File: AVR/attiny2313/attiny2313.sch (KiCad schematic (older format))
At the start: 7 parts

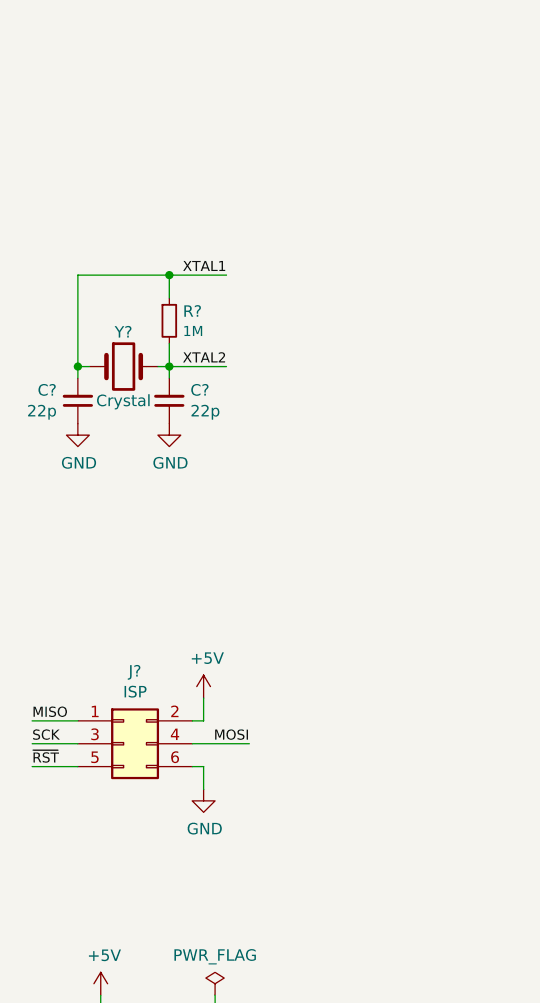
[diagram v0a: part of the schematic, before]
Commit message: Improving AVR templates
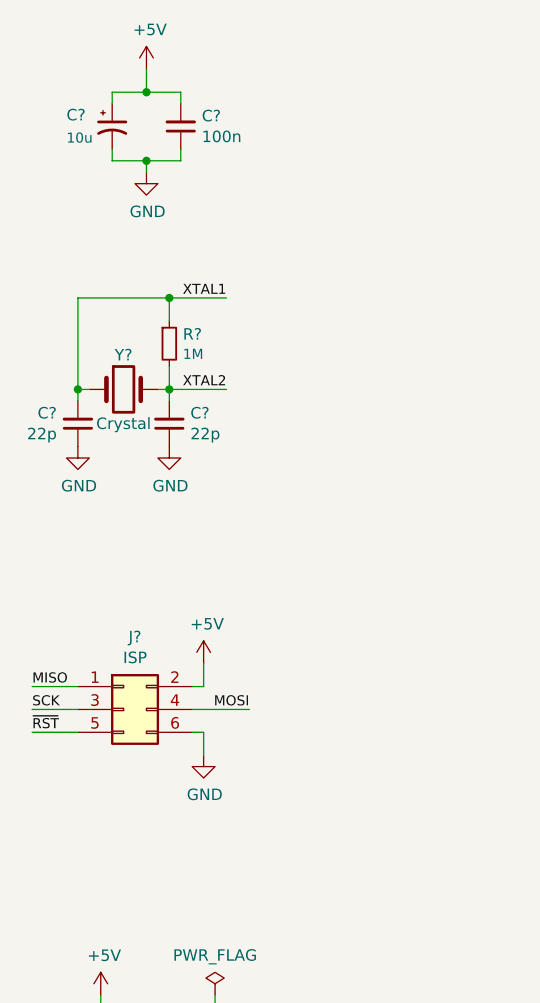
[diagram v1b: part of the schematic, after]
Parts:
- added C?: 10u, symbol Device:CP1_Small
- added C?: 100n, symbol Device:C_Small
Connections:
- net +5V: now also C?.1, C?.2
- net GND: now also C?.1, C?.2
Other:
- moved on the sheet: C?, J?, R?, Y?
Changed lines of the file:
@@
 EESchema Schematic File Version 4
-LIBS:atmega8-cache
+LIBS:attiny2313-cache
 EELAYER 26 0
 EELAYER END
@@
 $EndDescr
 Wire Wire Line
-	1750 2950 1700 2950
-Wire Wire Line
-	2100 2850 2100 2950
-Connection ~ 2100 2950
-Connection ~ 1700 2950
-Wire Wire Line
-	2050 2950 2100 2950
-Text Label 2350 2550 2    44   ~ 0
+	1750 3050 1700 3050
+Wire Wire Line
+	2100 2950 2100 3050
+Connection ~ 2100 3050
+Connection ~ 1700 3050
+Wire Wire Line
+	2050 3050 2100 3050
+Text Label 2350 2650 2    44   ~ 0
 XTAL1
-Text Label 2350 2950 2    44   ~ 0
+Text Label 2350 3050 2    44   ~ 0
 XTAL2
 Wire Wire Line
-	1700 2550 1700 2950
-Wire Wire Line
-	2350 2550 2100 2550
-Wire Wire Line
-	2100 2650 2100 2550
-Connection ~ 2100 2550
-Wire Wire Line
-	2100 2950 2100 3000
-Wire Wire Line
-	2100 2950 2350 2950
-Wire Wire Line
-	1700 2950 1700 3000
-Wire Wire Line
-	2100 2550 1700 2550
+	1700 2650 1700 3050
+Wire Wire Line
+	2350 2650 2100 2650
+Wire Wire Line
+	2100 2750 2100 2650
+Connection ~ 2100 2650
+Wire Wire Line
+	2100 3050 2100 3100
+Wire Wire Line
+	2100 3050 2350 3050
+Wire Wire Line
+	1700 3050 1700 3100
+Wire Wire Line
+	2100 2650 1700 2650
 $Comp
 L Device:Crystal Y?
 U 1 1 5B7974AC
-P 1900 2950
-F 0 "Y?" H 1900 3100 50  0000 C CNN
-F 1 "Crystal" H 1900 2800 50  0000 C CNN
-F 2 "" H 1900 2950 50  0001 C CNN
-F 3 "~" H 1900 2950 50  0001 C CNN
-	1    1900 2950
+P 1900 3050
+F 0 "Y?" H 1900 3200 50  0000 C CNN
+F 1 "Crystal" H 1900 2900 50  0000 C CNN
+F 2 "" H 1900 3050 50  0001 C CNN
+F 3 "~" H 1900 3050 50  0001 C CNN
+	1    1900 3050
 	1    0    0    -1
 $EndComp
@@
 L power:GND #PWR?
 U 1 1 5B79740B
-P 1700 3200
-F 0 "#PWR?" H 1700 2950 50  0001 C CNN
-F 1 "GND" H 1705 3027 50  0000 C CNN
-F 2 "" H 1700 3200 50  0001 C CNN
-F 3 "" H 1700 3200 50  0001 C CNN
-	1    1700 3200
+P 1700 3300
+F 0 "#PWR?" H 1700 3050 50  0001 C CNN
+F 1 "GND" H 1705 3127 50  0000 C CNN
+F 2 "" H 1700 3300 50  0001 C CNN
+F 3 "" H 1700 3300 50  0001 C CNN
+	1    1700 3300
 	1    0    0    -1
 $EndComp
@@
 L Device:C_Small C?
 U 1 1 5B7975FD
-P 1700 3100
-F 0 "C?" H 1608 3054 50  0000 R CNN
-F 1 "22p" H 1608 3145 50  0000 R CNN
-F 2 "" H 1700 3100 50  0001 C CNN
-F 3 "~" H 1700 3100 50  0001 C CNN
-	1    1700 3100
+P 1700 3200
+F 0 "C?" H 1608 3154 50  0000 R CNN
+F 1 "22p" H 1608 3245 50  0000 R CNN
+F 2 "" H 1700 3200 50  0001 C CNN
+F 3 "~" H 1700 3200 50  0001 C CNN
+	1    1700 3200
 	1    0    0    1
 $EndComp
@@
 L Device:C_Small C?
 U 1 1 5B7979A7
-P 2100 3100
-F 0 "C?" H 2008 3054 50  0000 R CNN
-F 1 "22p" H 2008 3145 50  0000 R CNN
-F 2 "" H 2100 3100 50  0001 C CNN
-F 3 "~" H 2100 3100 50  0001 C CNN
-	1    2100 3100
+P 2100 3200
+F 0 "C?" H 2008 3154 50  0000 R CNN
+F 1 "22p" H 2008 3245 50  0000 R CNN
+F 2 "" H 2100 3200 50  0001 C CNN
+F 3 "~" H 2100 3200 50  0001 C CNN
+	1    2100 3200
 	-1   0    0    1
 $EndComp
@@
 L power:GND #PWR?
 U 1 1 5B797A2C
-P 2100 3200
-F 0 "#PWR?" H 2100 2950 50  0001 C CNN
-F 1 "GND" H 2105 3027 50  0000 C CNN
-F 2 "" H 2100 3200 50  0001 C CNN
-F 3 "" H 2100 3200 50  0001 C CNN
-	1    2100 3200
+P 2100 3300
+F 0 "#PWR?" H 2100 3050 50  0001 C CNN
+F 1 "GND" H 2105 3127 50  0000 C CNN
+F 2 "" H 2100 3300 50  0001 C CNN
+F 3 "" H 2100 3300 50  0001 C CNN
+	1    2100 3300
 	1    0    0    -1
 $EndComp
@@
 L Device:R_Small R?
 U 1 1 5B797AEA
-P 2100 2750
-F 0 "R?" H 2159 2791 50  0000 L CNN
-F 1 "1M" H 2159 2704 44  0000 L CNN
-F 2 "" H 2100 2750 50  0001 C CNN
-F 3 "~" H 2100 2750 50  0001 C CNN
-	1    2100 2750
-	1    0    0    -1
-$EndComp
-Wire Wire Line
-	2200 4500 2250 4500
-Wire Wire Line
-	2250 4500 2250 4400
-Wire Wire Line
-	2250 4800 2250 4700
-Wire Wire Line
-	2250 4700 2200 4700
-Wire Wire Line
-	1700 4500 1500 4500
-Wire Wire Line
-	1700 4600 1500 4600
-Wire Wire Line
-	1700 4700 1500 4700
-Wire Wire Line
-	2200 4600 2450 4600
-Text Label 1500 4500 0    44   ~ 0
+P 2100 2850
+F 0 "R?" H 2159 2891 50  0000 L CNN
+F 1 "1M" H 2159 2804 44  0000 L CNN
+F 2 "" H 2100 2850 50  0001 C CNN
+F 3 "~" H 2100 2850 50  0001 C CNN
+	1    2100 2850
+	1    0    0    -1
+$EndComp
+Wire Wire Line
+	2200 4350 2250 4350
+Wire Wire Line
+	2250 4350 2250 4250
+Wire Wire Line
+	2250 4650 2250 4550
+Wire Wire Line
+	2250 4550 2200 4550
+Wire Wire Line
+	1700 4350 1500 4350
+Wire Wire Line
+	1700 4450 1500 4450
+Wire Wire Line
+	1700 4550 1500 4550
+Wire Wire Line
+	2200 4450 2450 4450
+Text Label 1500 4350 0    44   ~ 0
 MISO
-Text Label 1500 4600 0    44   ~ 0
+Text Label 1500 4450 0    44   ~ 0
 SCK
-Text Label 1500 4700 0    44   ~ 0
+Text Label 1500 4550 0    44   ~ 0
 ~RST
-Text Label 2450 4600 2    44   ~ 0
+Text Label 2450 4450 2    44   ~ 0
 MOSI
 $Comp
 L Connector_Generic:Conn_02x03_Odd_Even J?
 U 1 1 5B79766C
-P 1900 4600
-F 0 "J?" H 1950 4917 50  0000 C CNN
-F 1 "ISP" H 1950 4826 50  0000 C CNN
-F 2 "" H 1900 4600 50  0001 C CNN
-F 3 "~" H 1900 4600 50  0001 C CNN
-	1    1900 4600
+P 1900 4450
+F 0 "J?" H 1950 4767 50  0000 C CNN
+F 1 "ISP" H 1950 4676 50  0000 C CNN
+F 2 "" H 1900 4450 50  0001 C CNN
+F 3 "~" H 1900 4450 50  0001 C CNN
+	1    1900 4450
 	1    0    0    -1
 $EndComp
@@
 L power:GND #PWR?
 U 1 1 5B7976F0
-P 2250 4800
-F 0 "#PWR?" H 2250 4550 50  0001 C CNN
-F 1 "GND" H 2255 4627 50  0000 C CNN
-F 2 "" H 2250 4800 50  0001 C CNN
-F 3 "" H 2250 4800 50  0001 C CNN
-	1    2250 4800
+P 2250 4650
+F 0 "#PWR?" H 2250 4400 50  0001 C CNN
+F 1 "GND" H 2255 4477 50  0000 C CNN
+F 2 "" H 2250 4650 50  0001 C CNN
+F 3 "" H 2250 4650 50  0001 C CNN
+	1    2250 4650
 	1    0    0    -1
 $EndComp
@@
 L power:+5V #PWR?
 U 1 1 5B797725
-P 2250 4400
-F 0 "#PWR?" H 2250 4250 50  0001 C CNN
-F 1 "+5V" H 2265 4573 50  0000 C CNN
-F 2 "" H 2250 4400 50  0001 C CNN
-F 3 "" H 2250 4400 50  0001 C CNN
-	1    2250 4400
+P 2250 4250
+F 0 "#PWR?" H 2250 4100 50  0001 C CNN
+F 1 "+5V" H 2265 4423 50  0000 C CNN
+F 2 "" H 2250 4250 50  0001 C CNN
+F 3 "" H 2250 4250 50  0001 C CNN
+	1    2250 4250
 	1    0    0    -1
 $EndComp
@@
 Wire Wire Line
 	5400 2050 5400 2250
+$Comp
+L Device:CP1_Small C?
+U 1 1 5B842150
+P 1850 1900
+F 0 "C?" H 1650 1950 50  0000 L CNN
+F 1 "10u" H 1650 1850 44  0000 L CNN
+F 2 "" H 1850 1900 50  0001 C CNN
+F 3 "~" H 1850 1900 50  0001 C CNN
+	1    1850 1900
+	1    0    0    -1
+$EndComp
+$Comp
+L power:GND #PWR?
+U 1 1 5B84359D
+P 2000 2100
+F 0 "#PWR?" H 2000 1850 50  0001 C CNN
+F 1 "GND" H 2005 1927 50  0000 C CNN
+F 2 "" H 2000 2100 50  0001 C CNN
+F 3 "" H 2000 2100 50  0001 C CNN
+	1    2000 2100
+	1    0    0    -1
+$EndComp
+$Comp
+L power:+5V #PWR?
+U 1 1 5B844FE0
+P 2000 1650
+F 0 "#PWR?" H 2000 1500 50  0001 C CNN
+F 1 "+5V" H 2015 1823 50  0000 C CNN
+F 2 "" H 2000 1650 50  0001 C CNN
+F 3 "" H 2000 1650 50  0001 C CNN
+	1    2000 1650
+	1    0    0    -1
+$EndComp
+$Comp
+L Device:C_Small C?
+U 1 1 5B84504B
+P 2150 1900
+F 0 "C?" H 2058 1854 50  0000 R CNN
+F 1 "100n" H 2058 1945 50  0000 R CNN
+F 2 "" H 2150 1900 50  0001 C CNN
+F 3 "~" H 2150 1900 50  0001 C CNN
+	1    2150 1900
+	-1   0    0    1
+$EndComp
+Wire Wire Line
+	1850 2000 1850 2050
+Wire Wire Line
+	1850 2050 2000 2050
+Wire Wire Line
+	2150 2050 2150 2000
+Wire Wire Line
+	2000 2050 2000 2100
+Connection ~ 2000 2050
+Wire Wire Line
+	2000 2050 2150 2050
+Wire Wire Line
+	1850 1800 1850 1750
+Wire Wire Line
+	1850 1750 2000 1750
+Wire Wire Line
+	2150 1750 2150 1800
+Wire Wire Line
+	2000 1650 2000 1750
+Connection ~ 2000 1750
+Wire Wire Line
+	2000 1750 2150 1750
 $EndSCHEMATC

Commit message: Update to KiCad 5.1.7
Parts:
- U?: symbol MCU_Microchip_ATtiny:ATtiny2313-20MU -> attiny2313-rescue:ATtiny2313-20MU-MCU_Microchip_ATtiny
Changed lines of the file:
@@
 EESchema Schematic File Version 4
-LIBS:attiny2313-cache
-EELAYER 26 0
+EELAYER 30 0
 EELAYER END
 $Descr A4 11693 8268
@@
 	2300 5700 2300 5900
 $Comp
-L MCU_Microchip_ATtiny:ATtiny2313-20MU U?
+L attiny2313-rescue:ATtiny2313-20MU-MCU_Microchip_ATtiny U?
 U 1 1 5B848F14
 P 5400 3350
